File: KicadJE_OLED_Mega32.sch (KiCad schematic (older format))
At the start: 86 parts, among them J201 OLED, J202 ADC Input, J203 Out2, J204 Out1, J205 OUT1, J206 OUT2, J207 IN1, J208 IN2, J209 CV1, J210 CV2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

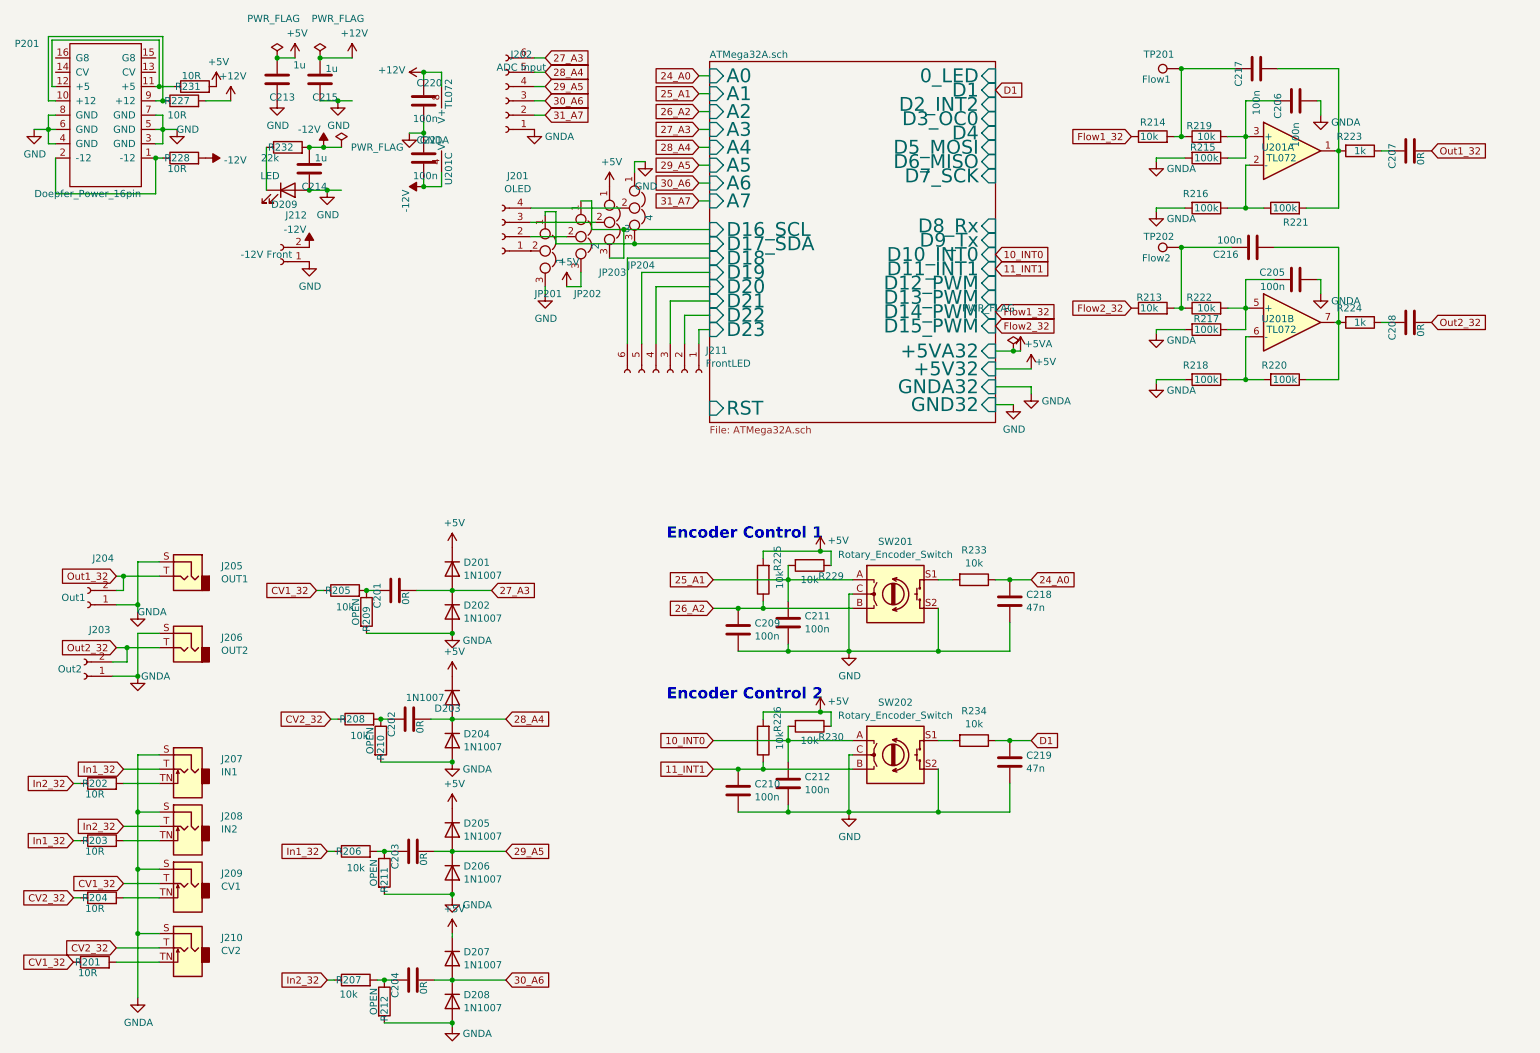
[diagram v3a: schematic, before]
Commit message: Added buffer for output
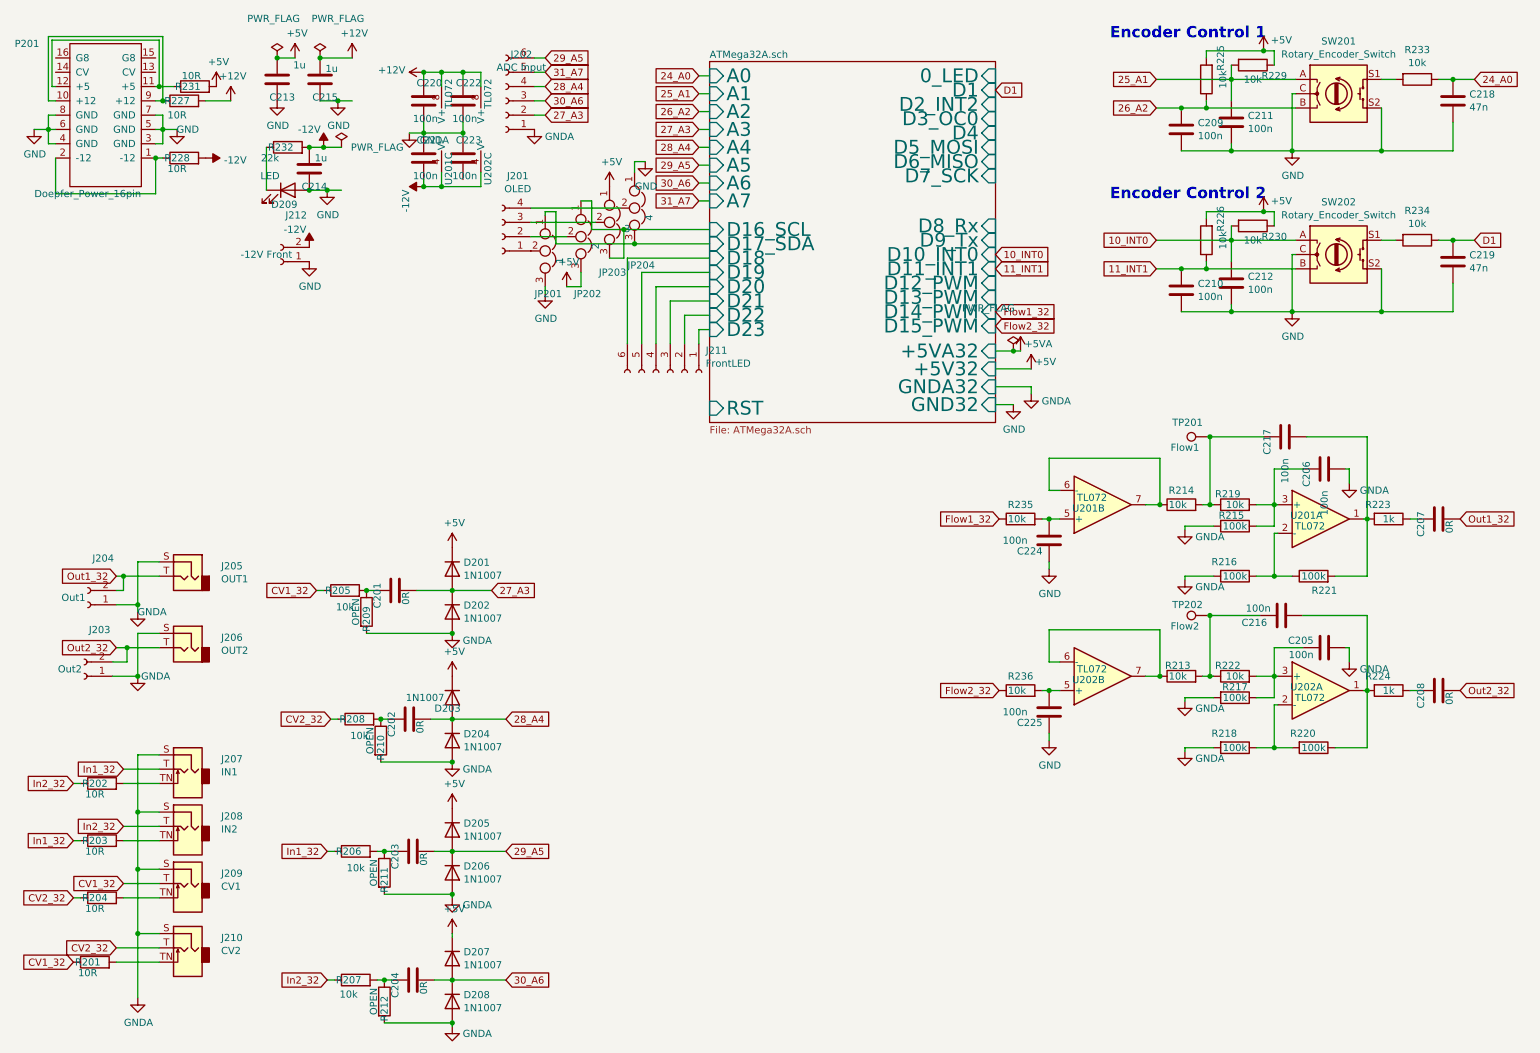
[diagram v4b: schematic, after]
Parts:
- added C222, C223, C224, C225: 100n, AJ:C_0805_AJ, symbol Device:C
- added R235, R236: 10k, AJ:R_0805_AJ, symbol Device:R
- added unit 2 of U201
- added unit 3 of U202
- added unit 2 of U202
- renumbered U201 to U202
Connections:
- net +12V: now also C222.1, U202.8 (V+)
- net -12V: now also U202.4 (V-)
- net 27_A3: now also J202.2 (Pin_2); no longer J202.6 (Pin_6)
- net 28_A4: now also J202.4 (Pin_4); no longer J202.5 (Pin_5)
- net 29_A5: now also J202.6 (Pin_6); no longer J202.4 (Pin_4)
- net 31_A7: now also J202.5 (Pin_5); no longer J202.2 (Pin_2)
- net Flow1_32: now also R235.1; no longer R214.1
- net Flow2_32: now also R236.1; no longer R213.1
- net GND: now also C224.2, C225.2
- net GNDA: now also C222.2, C223.1
- net at C205.1, R217.1, R222.2: now also U202.3 (+); no longer U202.5 (+)
- net at R218.1, R220.2: now also U202.2 (-); no longer U202.6 (-)
- net at C216.2, R220.1, R224.2: now also U202.1; no longer U202.7
- new net: R214.1, U201.6 (-), U201.7
- new net: R213.1, U202.6 (-), U202.7
- new net: C224.1, R235.2, U201.5 (+)
- new net: C225.1, R236.2, U202.5 (+)
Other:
- moved on the sheet: C205, C206, C207, C208, C209, C210, C211, C212, C216, C217, C218, C219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

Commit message: Components placed for KicadJE_OLED_Mega32
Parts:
- TP201, TP202: footprint TestPoint:TestPoint_THTPad_2.0x2.0mm_Drill1.0mm -> TestPoint:TestPoint_THTPad_1.0x1.0mm_Drill0.5mm
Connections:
- net -12V: now also C223.2
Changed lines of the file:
@@
 Wire Wire Line
 	9400 4100 9275 4100
-$Comp
-L Connector:TestPoint TP?
-U 1 1 60E39729
-P 8950 3475
-AR Path="/60E39729" Ref="TP?"  Part="1"
-AR Path="/608CA457/60E39729" Ref="TP201"  Part="1"
-F 0 "TP201" V 9050 3525 50  0000 L CNN
-F 1 "Flow1" V 8875 3550 50  0000 L CNN
-F 2 "TestPoint:TestPoint_THTPad_2.0x2.0mm_Drill1.0mm" H 9150 3475 50  0001 C CNN
-F 3 "~" H 9150 3475 50  0001 C CNN
-	1    8950 3475
-	0    -1   -1   0
-$EndComp
 Wire Wire Line
 	10400 4050 10350 4050
@@
 $Comp
 L Device:R R?
-U 1 1 60F63E8C
-P 10200 5250
-AR Path="/60F63E8C" Ref="R?"  Part="1"
-AR Path="/5C8C5FC0/60F63E8C" Ref="R?"  Part="1"
-AR Path="/5CAAE8D3/60F63E8C" Ref="R?"  Part="1"
-AR Path="/5E4B0DD9/60F63E8C" Ref="R?"  Part="1"
-AR Path="/5E62ACA1/60F63E8C" Ref="R?"  Part="1"
-AR Path="/5F49A670/60F63E8C" Ref="R?"  Part="1"
-AR Path="/608CA457/60F63E8C" Ref="R224"  Part="1"
-F 0 "R224" V 10100 5175 50  0000 C CNN
-F 1 "1k" V 10200 5250 50  0000 C CNN
-F 2 "AJ:R_0805_AJ" V 10130 5250 50  0001 C CNN
-F 3 "~" H 10200 5250 50  0001 C CNN
-	1    10200 5250
-	0    1    1    0
-$EndComp
-$Comp
-L Device:R R?
 U 1 1 60F63EA0
 P 9125 5650
@@
 F 0 "TP202" V 9025 4775 50  0000 L CNN
 F 1 "Flow2" V 8875 4800 50  0000 L CNN
-F 2 "TestPoint:TestPoint_THTPad_2.0x2.0mm_Drill1.0mm" H 9150 4725 50  0001 C CNN
+F 2 "TestPoint:TestPoint_THTPad_1.0x1.0mm_Drill0.5mm" H 9150 4725 50  0001 C CNN
 F 3 "~" H 9150 4725 50  0001 C CNN
 	1    8950 4725
@@
 $EndComp
 Wire Wire Line
-	9275 5150 9400 5150
-Wire Wire Line
 	9400 5150 9400 4950
 Wire Wire Line
@@
 	3725 925  3850 925
 Wire Wire Line
-	3575 1725 3850 1725
+	3575 1725 3725 1725
 Connection ~ 3575 1725
 Wire Wire Line
@@
 $EndComp
 Connection ~ 8600 5150
+Wire Wire Line
+	3725 1675 3725 1725
+Connection ~ 3725 1725
+Wire Wire Line
+	3725 1725 3850 1725
+$Comp
+L Connector:TestPoint TP?
+U 1 1 60E39729
+P 8950 3475
+AR Path="/60E39729" Ref="TP?"  Part="1"
+AR Path="/608CA457/60E39729" Ref="TP201"  Part="1"
+F 0 "TP201" V 9050 3525 50  0000 L CNN
+F 1 "Flow1" V 8875 3550 50  0000 L CNN
+F 2 "TestPoint:TestPoint_THTPad_1.0x1.0mm_Drill0.5mm" H 9150 3475 50  0001 C CNN
+F 3 "~" H 9150 3475 50  0001 C CNN
+	1    8950 3475
+	0    -1   -1   0
+$EndComp
+Wire Wire Line
+	9275 5150 9400 5150
+$Comp
+L Device:R R?
+U 1 1 60F63E8C
+P 10200 5250
+AR Path="/60F63E8C" Ref="R?"  Part="1"
+AR Path="/5C8C5FC0/60F63E8C" Ref="R?"  Part="1"
+AR Path="/5CAAE8D3/60F63E8C" Ref="R?"  Part="1"
+AR Path="/5E4B0DD9/60F63E8C" Ref="R?"  Part="1"
+AR Path="/5E62ACA1/60F63E8C" Ref="R?"  Part="1"
+AR Path="/5F49A670/60F63E8C" Ref="R?"  Part="1"
+AR Path="/608CA457/60F63E8C" Ref="R224"  Part="1"
+F 0 "R224" V 10100 5175 50  0000 C CNN
+F 1 "1k" V 10200 5250 50  0000 C CNN
+F 2 "AJ:R_0805_AJ" V 10130 5250 50  0001 C CNN
+F 3 "~" H 10200 5250 50  0001 C CNN
+	1    10200 5250
+	0    1    1    0
+$EndComp
 $EndSCHEMATC
